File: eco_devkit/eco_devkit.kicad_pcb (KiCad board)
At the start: 2 copper layers, 24 parts, among them J10 Micro_SD_Card_Det1, J11 DISPLAY FFC, Q5 T2N7002AK,LM, Q6 SL2301S, U2 LTR-329ALS-01, U3 MC3419

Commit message: Add digital peripherals layout.
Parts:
- added BZ1: WT-1205, lib:buzzer, F.Cu at (211.0, 127.0)
- added C21: 0.1u, Capacitor_SMD:C_0402_1005Metric, F.Cu at (269.0, 152.0)
- added C22: 0.1u, Capacitor_SMD:C_0402_1005Metric, F.Cu at (269.0, 158.5)
- added C23: 0.1u, Capacitor_SMD:C_0402_1005Metric, F.Cu at (269.0, 165.0)
- added C24: 0.1u, Capacitor_SMD:C_0402_1005Metric, F.Cu at (269.0, 172.0)
- added D2: LED_Red, LED_SMD:LED_1206_3216Metric, F.Cu at (237.5, 124.0)
- added D3: LED_Green, LED_SMD:LED_1206_3216Metric, F.Cu at (237.5, 128.0)
- added D4: LED_Blue, LED_SMD:LED_1206_3216Metric, F.Cu at (237.5, 131.8)
- added D5: LED_Yellow, LED_SMD:LED_1206_3216Metric, F.Cu at (237.5, 135.5)
- added D6: WS2812B, LED_SMD:LED_WS2812B_PLCC4_5.0x5.0mm_P3.2mm, F.Cu at (238.0, 149.5)
- added D7: TSAL4400, LED_THT:LED_D3.0mm_Horizontal_O1.27mm_Z2.0mm, F.Cu at (208.2, 168.2)
- added J3: ADC_SEL1, Connector_PinSocket_2.54mm:PinSocket_1x02_P2.54mm_Vertical, F.Cu at (265.5, 129.0)
- added J4: BluetoothHeader, Connector_PinHeader_2.54mm:PinHeader_2x04_P2.54mm_Vertical, F.Cu at (236.5, 164.9)
- added Q1: MOSFET, Package_TO_SOT_SMD:SOT-23, F.Cu at (264.7, 123.9)
- added Q2: MMBT3904, Package_TO_SOT_SMD:SOT-523, F.Cu at (223.0, 125.1)
- added Q3: MOSFET, Package_TO_SOT_SMD:SOT-23, F.Cu at (209.0, 159.5)
- added Q4: OP598A, LED_THT:LED_D3.0mm_Horizontal_O1.27mm_Z2.0mm_Clear, F.Cu at (214.2, 168.2)
- added R12: 150, Resistor_SMD:R_0402_1005Metric, F.Cu at (241.5, 124.0)
- added R13: 150, Resistor_SMD:R_0402_1005Metric, F.Cu at (241.5, 128.0)
- added R14: 33, Resistor_SMD:R_0402_1005Metric, F.Cu at (241.5, 131.8)
- added R15: 150, Resistor_SMD:R_0402_1005Metric, F.Cu at (241.5, 135.5)
- added R16: 10k, Resistor_SMD:R_0402_1005Metric, F.Cu at (267.5, 152.0)
- added R17: 10k, Resistor_SMD:R_0402_1005Metric, F.Cu at (267.5, 158.5)
- added R18: 10k, Resistor_SMD:R_0402_1005Metric, F.Cu at (267.5, 165.0)
- added R19: 10k, Resistor_SMD:R_0402_1005Metric, F.Cu at (267.5, 172.0)
- added R20: 330, Resistor_SMD:R_0402_1005Metric, F.Cu at (240.5, 144.8)
- added R21: 100, Resistor_SMD:R_0402_1005Metric, F.Cu at (261.8, 123.5)
- added R22: 1k, Resistor_SMD:R_0402_1005Metric, F.Cu at (222.5, 122.5)
- added R23: 330, Resistor_SMD:R_0402_1005Metric, F.Cu at (208.1, 156.0)
- added R24: 10k, Resistor_SMD:R_0402_1005Metric, F.Cu at (233.0, 167.5)
- added R25: 220, Resistor_SMD:R_0402_1005Metric, F.Cu at (211.4, 161.5)
- added R26: 10k, Resistor_SMD:R_0402_1005Metric, F.Cu at (242.5, 165.0)
- added R27: 10k, Resistor_SMD:R_0402_1005Metric, F.Cu at (216.8, 161.5)
- added R28: 10k, Resistor_SMD:R_0402_1005Metric, F.Cu at (242.5, 170.0)
- added R29: 10k, Resistor_SMD:R_0402_1005Metric, F.Cu at (233.0, 172.5)
- added SW3: PTS636, Button_Switch_SMD:SW_Tactile_SPST_NO_Straight_CK_PTS636Sx25SMTRLFS, F.Cu at (262.0, 151.5)
- added SW4: PTS636, Button_Switch_SMD:SW_Tactile_SPST_NO_Straight_CK_PTS636Sx25SMTRLFS, F.Cu at (262.0, 158.0)
- added SW5: PTS636, Button_Switch_SMD:SW_Tactile_SPST_NO_Straight_CK_PTS636Sx25SMTRLFS, F.Cu at (262.0, 164.5)
- added SW6: PTS636, Button_Switch_SMD:SW_Tactile_SPST_NO_Straight_CK_PTS636Sx25SMTRLFS, F.Cu at (262.0, 171.5)
- moved C45 14.9 mm to (38.2, 179.1)
- moved C46 14.9 mm to (40.2, 179.1)
- moved C47 14.9 mm to (42.2, 179.1)
- moved J10 14.9 mm to (54.8, 162.6)
- moved C41 14.9 mm to (44.8, 164.6)
- moved C42 14.9 mm to (32.6, 162.8)
- moved C43 14.9 mm to (33.2, 173.1)
- moved C44 14.9 mm to (33.2, 174.1)
- moved C48 14.9 mm to (33.2, 186.6)
- moved C49 14.9 mm to (33.2, 185.6)
- moved J11 14.9 mm to (28.7, 179.1)
- moved JP1 14.9 mm to (48.0, 173.3)
- moved Q5 14.9 mm to (45.7, 189.1)
- moved Q6 14.9 mm to (44.6, 183.0)
- moved R42 14.9 mm to (44.8, 161.6)
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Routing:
- net Net-(D7-K): track 0.00 -> 7.78 mm
- net Net-(D7-A): track 0.00 -> 6.44 mm
- net IR_RX: track 0.00 -> 6.16 mm
- net Net-(BZ1--): track 0.00 -> 5.52 mm
- net GPIO_MOSFET_CONECTOR_OUT: track 0.00 -> 4.45 mm
- net PIN_BTN4: track 0.00 -> 3.13 mm
- net PIN_BTN3: track 0.00 -> 3.13 mm
- net PIN_BTN2: track 0.00 -> 3.13 mm
- net PIN_BTN1: track 0.00 -> 3.13 mm
- net Net-(J4-Pin_2): track 0.00 -> 3.02 mm
- net Net-(J4-Pin_6): track 0.00 -> 2.99 mm
- net PIN_WIFI_RESET_BL: track 0.00 -> 2.97 mm
- net Net-(J4-Pin_3): track 0.00 -> 2.97 mm
- net Net-(D6-DIN): track 0.00 -> 2.58 mm
- net Net-(D5-A): track 0.00 -> 2.09 mm
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
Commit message: Add probe.
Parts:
- added C26: 15p, Capacitor_SMD:C_0603_1608Metric, F.Cu at (110.0, 84.7)
- added C27: 15p, Capacitor_SMD:C_0603_1608Metric, F.Cu at (117.0, 86.2)
- added C28: 100n, Capacitor_SMD:C_0402_1005Metric, F.Cu at (109.5, 61.0)
- added C29: 10u, Capacitor_SMD:C_0402_1005Metric, F.Cu at (120.0, 63.0)
- added C30: 100n, Capacitor_SMD:C_0402_1005Metric, F.Cu at (115.5, 67.5)
- added C31: 100n, Capacitor_SMD:C_0402_1005Metric, F.Cu at (119.5, 67.5)
- added C32: 1u, Capacitor_SMD:C_0402_1005Metric, F.Cu at (119.9, 83.5)
- added C33: 100n, Capacitor_SMD:C_0402_1005Metric, F.Cu at (112.0, 72.5)
- added C34: 1u, Capacitor_SMD:C_0402_1005Metric, F.Cu at (112.0, 78.0)
- added C35: 100n, Capacitor_SMD:C_0402_1005Metric, F.Cu at (120.5, 67.5)
- added C36: 100n, Capacitor_SMD:C_0402_1005Metric, F.Cu at (121.5, 67.5)
- added C37: 100n, Capacitor_SMD:C_0402_1005Metric, F.Cu at (122.0, 74.5)
- added C38: 100n, Capacitor_SMD:C_0402_1005Metric, F.Cu at (122.0, 78.0)
- added C39: 100n, Capacitor_SMD:C_0402_1005Metric, F.Cu at (116.5, 67.5)
- added C40: 100n, Capacitor_SMD:C_0402_1005Metric, F.Cu at (118.5, 83.5)
- added D8: SB120, Diode_SMD:D_SOD-123F, F.Cu at (121.4, 61.0)
- added J2: Conn_02x20_Counter_Clockwise, Connector_PinHeader_2.54mm:PinHeader_2x20_P2.54mm_Vertical, F.Cu at (174.2, 126.0)
- added J8: USB_C_Receptacle_USB2.0_16P, lib:UJ20-C-H-G-SMT-1-P16-TR, F.Cu at (118.1, 50.2)
- added J9: SWD Interface, Connector_PinSocket_2.54mm:PinSocket_1x06_P2.54mm_Vertical, F.Cu at (105.0, 72.8)
- added MEM1: AT25EU0011A-SSHN-T, Footprint-FlashMEM:SOIC127P790X216-8N, F.Cu at (108.0, 65.0)
- added R35: DNF, Resistor_SMD:R_0402_1005Metric, F.Cu at (106.0, 61.0)
- added R36: 5.1k, Resistor_SMD:R_0402_1005Metric, F.Cu at (118.5, 61.5)
- added R37: 5.1k, Resistor_SMD:R_0402_1005Metric, F.Cu at (115.0, 61.5)
- added R38: 1k, Resistor_SMD:R_0402_1005Metric, F.Cu at (117.0, 83.2)
- added R39: 10k, Resistor_SMD:R_0402_1005Metric, F.Cu at (120.9, 83.5)
- added R40: 27, Resistor_SMD:R_0402_1005Metric, F.Cu at (117.5, 67.5)
- added R41: 27, Resistor_SMD:R_0402_1005Metric, F.Cu at (118.5, 67.5)
- added U1: RP2040, Package_DFN_QFN:QFN-56-1EP_7x7mm_P0.4mm_EP3.2x3.2mm_ThermalVias, F.Cu at (116.9, 75.9)
- added Y2: ABM8-272-T3, lib:ABM8-272-T3, F.Cu at (113.0, 84.2)
- moved R19 149.7 mm to (166.5, 61.5), turned to 0 degrees
- moved C24 149.6 mm to (166.5, 63.0), turned to 180 degrees
- moved SW6 149.6 mm to (167.0, 56.0), turned to -90 degrees
- moved R45 141.8 mm to (138.5, 68.8), turned to 90 degrees
- moved U3 141.2 mm to (138.0, 71.0), turned to 180 degrees
- moved U2 141.1 mm to (137.7, 74.6), turned to 90 degrees
- moved R44 140.4 mm to (137.5, 68.8), turned to 90 degrees
- moved R18 139.8 mm to (173.5, 61.5), turned to 0 degrees
- moved C23 139.7 mm to (173.5, 63.0), turned to 180 degrees
- moved SW5 139.7 mm to (174.0, 56.0), turned to -90 degrees
- moved C42 138.4 mm to (136.0, 70.8), turned to 90 degrees
- moved R17 130.6 mm to (180.0, 61.5), turned to 0 degrees
- moved SW4 130.6 mm to (180.5, 56.0), turned to -90 degrees
- moved C22 130.5 mm to (180.0, 63.0), turned to 180 degrees
- moved R48 122.1 mm to (124.3, 95.5), turned to -90 degrees
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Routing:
- net +3V3: track 0.00 -> 32.5 mm
- net /Debug Probe/QSPI_SS: track 0.00 -> 23.6 mm
- net /Debug Probe/RESET: track 0.00 -> 21.0 mm, vias 0 -> 1
- net /Debug Probe/SD1: track 0.00 -> 19.3 mm
- net /Debug Probe/SD2: track 0.00 -> 17.9 mm
- net /Debug Probe/SWDIO: track 0.00 -> 15.4 mm, vias 0 -> 1
- net /Debug Probe/SWCLK: track 0.00 -> 15.0 mm, vias 0 -> 1
- net +1V1: track 0.00 -> 14.5 mm
- net Net-(D8-A): track 0.00 -> 12.5 mm
- net /Debug Probe/SD3: track 0.00 -> 11.4 mm
- net /Debug Probe/QSPI_SCLK: track 0.00 -> 9.81 mm
- net /Debug Probe/XIN: track 0.00 -> 9.17 mm
- net /Debug Probe/SD0: track 0.00 -> 8.36 mm
- net Net-(C27-Pad2): track 0.00 -> 6.96 mm
- net Net-(U1-USB_DP): track 0.00 -> 4.65 mm
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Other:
- board outline added: 100 x 82 mm

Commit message: Placement v1.
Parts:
- added C1: 15p, Capacitor_SMD:C_0402_1005Metric, F.Cu at (124.2, 92.8)
- added C10: 4.7u, Capacitor_SMD:C_0402_1005Metric, F.Cu at (135.2, 70.4)
- added C11: 100n, Capacitor_SMD:C_0402_1005Metric, F.Cu at (116.4, 76.8)
- added C12: 100n, Capacitor_SMD:C_0402_1005Metric, F.Cu at (125.0, 68.6)
- added C13: 100n, Capacitor_SMD:C_0402_1005Metric, F.Cu at (116.4, 72.4)
- added C14: 100n, Capacitor_SMD:C_0402_1005Metric, F.Cu at (116.3, 74.5)
- added C15: 100n, Capacitor_SMD:C_0402_1005Metric, F.Cu at (116.3, 79.1)
- added C16: 100n, Capacitor_SMD:C_0402_1005Metric, F.Cu at (120.9, 84.2)
- added C17: 100n, Capacitor_SMD:C_0402_1005Metric, F.Cu at (122.8, 84.2)
- added C18: 100n, Capacitor_SMD:C_0402_1005Metric, F.Cu at (134.2, 75.0)
- added C19: 100n, Capacitor_SMD:C_0402_1005Metric, F.Cu at (134.3, 73.9)
- added C2: 15p, Capacitor_SMD:C_0402_1005Metric, F.Cu at (118.8, 92.7)
- added C20: 100n, Capacitor_SMD:C_0402_1005Metric, F.Cu at (134.2, 80.4)
- added C25: 1u, Capacitor_SMD:C_0402_1005Metric, F.Cu at (159.0, 121.0)
- added C3: 10u, Capacitor_SMD:C_0402_1005Metric, F.Cu at (111.8, 57.9)
- added C4: 100n, Capacitor_SMD:C_0402_1005Metric, F.Cu at (124.9, 64.1)
- added C5: 10u, Capacitor_SMD:C_0402_1005Metric, F.Cu at (111.6, 53.5)
- added C6: 4.7u, Capacitor_SMD:C_0402_1005Metric, F.Cu at (134.3, 72.8)
- added C7: 4.7u, Capacitor_SMD:C_0402_1005Metric, F.Cu at (130.5, 68.7)
- added C8: 100n, Capacitor_SMD:C_0402_1005Metric, F.Cu at (134.2, 76.5)
- added C9: 4.7u, Capacitor_SMD:C_0402_1005Metric, F.Cu at (125.1, 84.2)
- added D1: SB120, Diode_SMD:D_SOD-123F, F.Cu at (115.3, 60.2)
- added FLASH_MEMORY_8MB1: W25Q80DVSSIG, Package_SON:WSON-8-1EP_6x5mm_P1.27mm_EP3.4x4.3mm, F.Cu at (120.5, 66.5)
- added J1: USB_C_Receptacle_USB2.0_16P, lib:UJ20-C-H-G-SMT-1-P16-TR, F.Cu at (126.6, 50.0)
- added J5: ADC_SEL1, Connector_PinHeader_2.54mm:PinHeader_1x02_P2.54mm_Vertical, F.Cu at (188.5, 115.0)
- added J6: ADC_SEL1, Connector_PinHeader_2.54mm:PinHeader_1x02_P2.54mm_Vertical, F.Cu at (185.0, 115.0)
- added J7: ADC_SEL1, Connector_PinHeader_2.54mm:PinHeader_1x02_P2.54mm_Vertical, F.Cu at (181.5, 115.0)
- added L1: 3.3u, Inductor_SMD:L_0402_1005Metric, F.Cu at (129.0, 69.1)
- added MK1: MIC, EcoDevkit:MIC_CMEJ-0415-42-P, F.Cu at (159.0, 125.0)
- added NCP1: NCP1117ST50T3G, lib:NCP1117ST50T3G, F.Cu at (116.7, 53.9)
- added R1: 0, Resistor_SMD:R_0402_1005Metric, F.Cu at (115.0, 65.7)
- added R10: 27, Resistor_SMD:R_0402_1005Metric, F.Cu at (126.2, 68.6)
- added R11: 27, Resistor_SMD:R_0402_1005Metric, F.Cu at (127.5, 68.6)
- added R2: 0, Resistor_SMD:R_0402_1005Metric, F.Cu at (115.0, 64.6)
- added R3: 5.1k, Resistor_SMD:R_0402_1005Metric, F.Cu at (128.3, 59.1)
- added R30: 1k, Resistor_SMD:R_0402_1005Metric, F.Cu at (185.0, 126.0)
- added R31: 1k, Resistor_SMD:R_0402_1005Metric, F.Cu at (174.5, 126.0)
- added R32: 33k, Resistor_SMD:R_0402_1005Metric, F.Cu at (168.0, 120.0)
- added R33: 500k, OptoDevice:R_LDR_5.1x4.3mm_P3.4mm_Vertical, F.Cu at (168.0, 123.0)
- added R34: 2.2k, Resistor_SMD:R_0402_1005Metric, F.Cu at (159.0, 119.5)
- added R4: 5.1k, Resistor_SMD:R_0402_1005Metric, F.Cu at (124.3, 59.1)
- added R5: 10k, Resistor_SMD:R_0402_1005Metric, F.Cu at (115.0, 63.6)
- added R6: 1k, Resistor_SMD:R_0402_1005Metric, F.Cu at (125.4, 92.8)
- added R7: 1k, Resistor_SMD:R_0402_1005Metric, F.Cu at (117.6, 92.7)
- added R8: 33, Resistor_SMD:R_0402_1005Metric, F.Cu at (134.3, 71.6)
- added R9: 1k, Resistor_SMD:R_0402_1005Metric, F.Cu at (115.0, 66.7)
- added RP2350B1: RP2350B1, lib:RP2350B_QFN-80_EP_10.573x10.573_Pitch0.4mm, F.Cu at (123.6, 76.7)
- added RV1: 100k, EcoDevkit:TRIM_TC33X-2-203E, F.Cu at (188.0, 124.5)
- added RV2: 100k, EcoDevkit:TRIM_TC33X-2-203E, F.Cu at (177.5, 124.5)
- added SW1: BOOT, Button_Switch_SMD:SW_Tactile_SPST_NO_Straight_CK_PTS636Sx25SMTRLFS, F.Cu at (112.6, 73.4)
- added SW2: RESET, Button_Switch_SMD:SW_Tactile_SPST_NO_Straight_CK_PTS636Sx25SMTRLFS, F.Cu at (112.8, 92.7)
- added Y1: Crystal_GND24, lib:ABM8-272-T3, F.Cu at (121.5, 93.4)
- J11: footprint EcoDevkit:AMPHENOL_SFV28R-2STE1HLF -> EcoDevkit:FPC_30
- moved J2 96.2 mm to (103.1, 61.2), turned to 0 degrees
- moved J10 43.1 mm to (117.0, 120.8), turned to 0 degrees
- moved D2 42.7 mm to (164.5, 95.8), turned to 90 degrees
- moved D3 39.9 mm to (168.5, 95.8), turned to 90 degrees
- moved SW3 39.8 mm to (192.0, 95.5), turned to 180 degrees
- moved R12 38.1 mm to (164.5, 91.8), turned to 90 degrees
- moved R44 38.1 mm to (119.0, 102.0), turned to 180 degrees
- moved D4 37.9 mm to (172.3, 95.8), turned to 90 degrees
- moved R45 37.7 mm to (119.0, 101.0), turned to 180 degrees
- moved J3 37.2 mm to (162.9, 54.2), turned to 90 degrees
- moved J9 37.1 mm to (142.1, 72.0)
- moved R42 36.5 mm to (118.0, 110.8), turned to -90 degrees
- moved D5 36.5 mm to (176.0, 95.8), turned to 90 degrees
- moved C42 36.0 mm to (121.0, 103.5), turned to 180 degrees
- moved SW4 34.9 mm to (192.0, 89.0), turned to 180 degrees
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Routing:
- net +3V3: track 32.5 -> 76.5 mm
- net RUN: track 0.00 -> 17.3 mm
- net +1V1: track 14.5 -> 30.8 mm
- net PROBE_GPIO4/UART_TX: track 0.00 -> 16.1 mm
- net Net-(D1-A): track 0.00 -> 15.5 mm
- net /MCU/USB_D-: track 0.00 -> 13.8 mm
- net /MCU/XIN: track 0.00 -> 13.5 mm
- net /MCU/USB_D+: track 0.00 -> 13.5 mm
- net /MCU/QSPI_SS: track 0.00 -> 12.6 mm
- net /MCU/XOUT: track 0.00 -> 11.3 mm
- net /MCU/QSPI_SD1: track 0.00 -> 10.7 mm
- net Net-(RP2350B1-VREG_AVDD): track 0.00 -> 9.75 mm
- net /MCU/QSPI_SD2: track 0.00 -> 7.97 mm
- net Net-(R7-Pad2): track 0.00 -> 7.02 mm
- net +VBUS: track 0.00 -> 6.81 mm
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- added copper zone on F.Cu, net (none)
- added copper zone on F.Cu, net +3V3
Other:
- board size 100 x 82 mm -> 98.5 x 78 mm

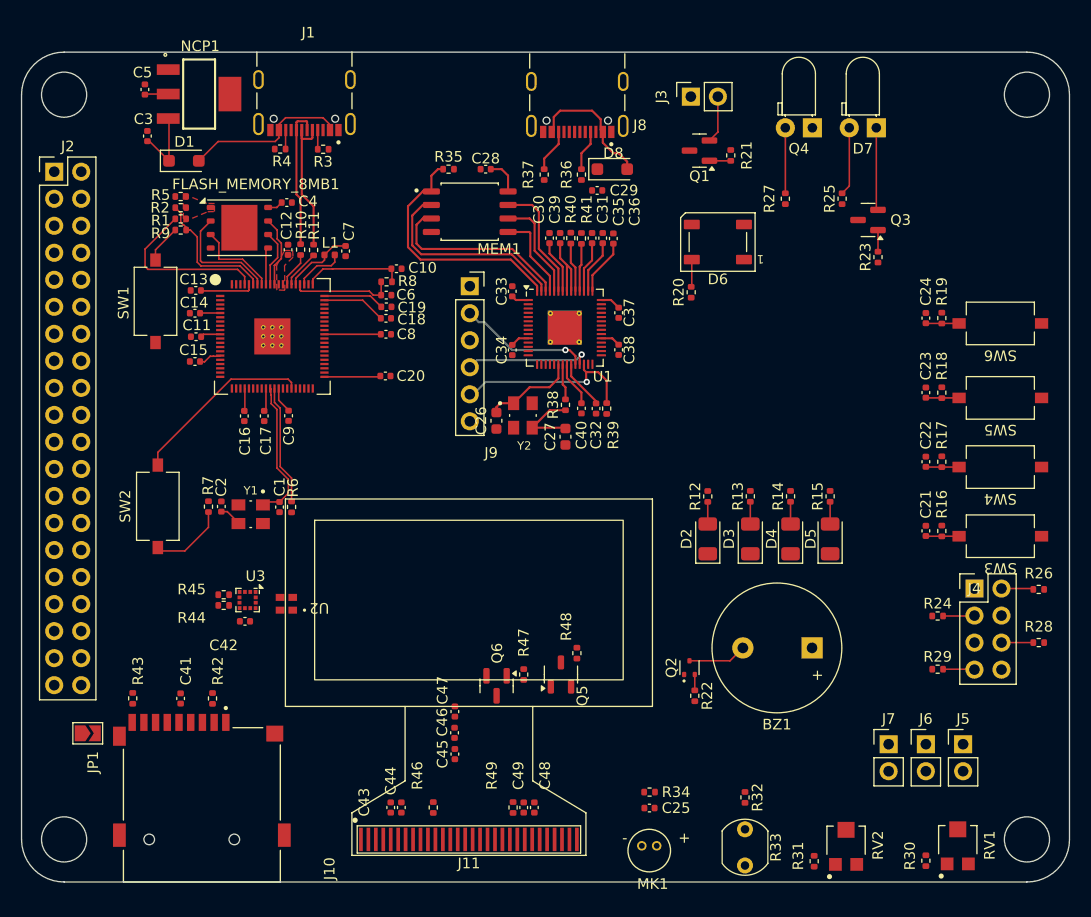
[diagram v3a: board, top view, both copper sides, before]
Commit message: fix:adjustments to component placement and routing
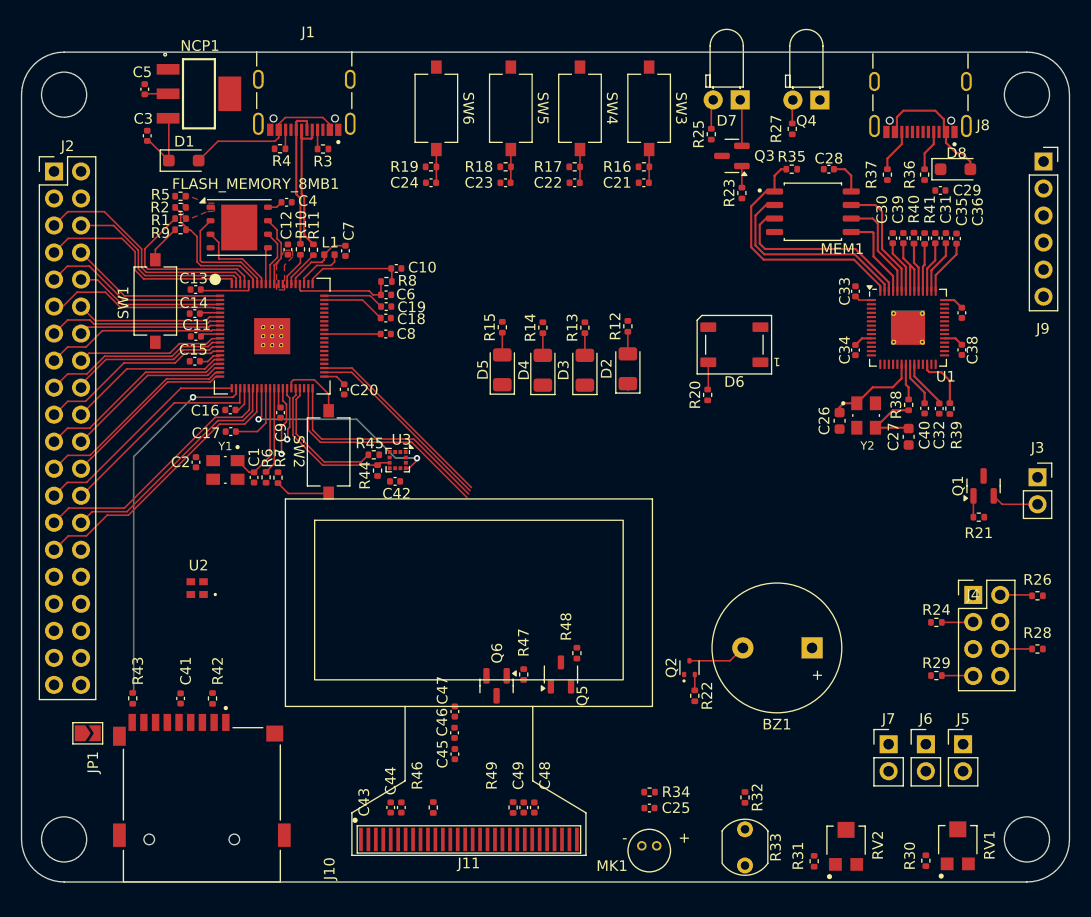
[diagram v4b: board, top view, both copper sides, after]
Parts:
- moved SW6 56.7 mm to (139.0, 55.3), turned to -90 degrees
- moved J9 55.2 mm to (196.1, 60.3)
- moved SW5 53.5 mm to (146.0, 55.3), turned to -90 degrees
- moved SW3 52.0 mm to (159.0, 55.3), turned to -90 degrees
- moved SW4 51.9 mm to (152.5, 55.3), turned to -90 degrees
- moved R19 50.1 mm to (138.5, 60.8), turned to 0 degrees
- moved J3 48.4 mm to (195.5, 90.0), turned to 0 degrees
- moved C24 48.2 mm to (138.5, 62.3), turned to 180 degrees
- moved R18 46.2 mm to (145.5, 60.8), turned to 0 degrees
- moved R17 44.3 mm to (152.0, 60.8), turned to 0 degrees
- moved R16 44.2 mm to (158.5, 60.8), turned to 0 degrees
- moved C23 44.2 mm to (145.5, 62.3), turned to 180 degrees
- moved C22 42.2 mm to (152.0, 62.3), turned to 180 degrees
- moved C21 42.1 mm to (158.5, 62.3), turned to 180 degrees
- moved Q1 41.3 mm to (190.4, 90.8), turned to 90 degrees
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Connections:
- J2 pad 21: PROBE_GPIO2/SWCLK -> /MCU/GPIO17
- J2 pad 22: SWD -> ACCEL_SCK
- J2 pad 23: RUN -> ACCEL_MOSI
- J2 pad 24: GPIO43_ADC3 -> ACCEL_MISO
- J2 pad 25: GPIO46_ADC6 -> GPIO21
- J2 pad 26: GPIO45_ADC5 -> /MCU/GPIO23
- J2 pad 27: GPIO44_ADC4 -> /MCU/GPIO24
- J2 pad 28: GPIO43_ADC3 -> /MCU/GPIO25
- J2 pad 29: GPIO42_ADC2 -> PIN_BUZZER
- J2 pad 30: GPIO41_ADC1 -> GPIO40_ADC0
- J2 pad 31: GPIO40_ADC0 -> GPIO41_ADC1
- J2 pad 32: PIN_BUZZER -> GPIO42_ADC2
- J2 pad 33: /MCU/GPIO25 -> GPIO43_ADC3
- J2 pad 34: /MCU/GPIO24 -> GPIO44_ADC4
- J2 pad 35: /MCU/GPIO23 -> GPIO45_ADC5
- J2 pad 36: GPIO21 -> GPIO46_ADC6
- J2 pad 37: ACCEL_MISO -> PROBE_GPIO2/SWCLK
- J2 pad 38: ACCEL_MOSI -> SWD
- J2 pad 39: ACCEL_SCK -> RUN
- J2 pad 40: /MCU/GPIO17 -> GPIO43_ADC3
- RP2350B1 pad 30: /MCU/XOUT -> /MCU/XIN
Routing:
- net GPIO22: track 0.00 -> 34.8 mm, vias 0 -> 1
- net PIN_BUZZER: track 0.00 -> 26.7 mm
- net /MCU/GPIO24: track 0.00 -> 24.8 mm
- net /MCU/GPIO25: track 0.00 -> 22.7 mm
- net POBRE_GPIO5/UART_RX: track 0.00 -> 22.3 mm
- net PIN_LED_RED: track 0.00 -> 22.2 mm
- net PIN_LED_GREEN: track 0.00 -> 21.6 mm
- net ACCEL_CS: track 0.00 -> 21.0 mm, vias 0 -> 2
- net GPIO21: track 0.00 -> 20.9 mm
- net /MCU/GPIO3: track 0.10 -> 20.4 mm
- net /MCU/GPIO23: track 0.00 -> 19.9 mm
- net ACCEL_MOSI: track 0.00 -> 19.4 mm
- net PIN_LED_YELLOW: track 0.00 -> 19.0 mm
- net PIN_LED_BLUE: track 0.00 -> 18.7 mm
- net /MCU/GPIO17: track 0.00 -> 18.6 mm
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
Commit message: Update layout
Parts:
- moved J3 47.7 mm to (166.0, 52.5), turned to 90 degrees
- moved Q4 47.0 mm to (194.7, 97.3), turned to 90 degrees
- moved D7 44.5 mm to (194.7, 89.8), turned to 90 degrees
- moved R27 42.2 mm to (191.9, 94.7), turned to 180 degrees
- moved R21 41.0 mm to (169.8, 58.0), turned to 90 degrees
- moved Q1 40.7 mm to (166.8, 57.6), turned to 180 degrees
- moved R25 39.6 mm to (191.4, 87.0), turned to 0 degrees
- moved Q3 37.0 mm to (189.4, 89.0), turned to 90 degrees
- moved R23 32.3 mm to (185.9, 89.9), turned to 0 degrees
- moved C43 2.20 mm to (132.5, 121.0), turned to 180 degrees
- moved C48 1.52 mm to (148.2, 119.5), turned to -90 degrees
- moved C49 1.52 mm to (147.2, 119.5), turned to -90 degrees
- moved R49 1.52 mm to (146.2, 119.5), turned to -90 degrees
- moved R45 1.11 mm to (132.0, 87.8), turned to -90 degrees
- moved D6 1.00 mm to (167.0, 78.5)
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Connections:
- J2 pad 18: /MCU/GPIO14 -> DISPLAY_CS
- J2 pad 20: /MCU/GPIO16 -> IR_RX
- J2 pad 21: /MCU/GPIO17 -> IR_TX
- RP2350B1 pad 13: /MCU/GPIO14 -> DISPLAY_CS
- RP2350B1 pad 16: /MCU/GPIO16 -> IR_RX
- RP2350B1 pad 17: /MCU/GPIO17 -> IR_TX
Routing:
- net IR_RX: track 2.23 -> 138.4 mm, vias 0 -> 2
- net IR_TX: track 0.00 -> 132.9 mm, vias 0 -> 2
- net DISPLAY_EN: track 17.4 -> 113.0 mm, vias 0 -> 2
- net DISPLAY_CS: track 0.00 -> 86.6 mm, vias 0 -> 2
- net POBRE_GPIO5/UART_RX: track 22.3 -> 107.6 mm, vias 0 -> 2
- net PROBE_GPIO4/UART_TX: track 16.1 -> 97.3 mm, vias 0 -> 2
- net DISPLAY_RST: track 13.9 -> 91.9 mm, vias 0 -> 2
- net PROBE_GPIO2/SWCLK: track 6.55 -> 73.4 mm, vias 1 -> 2
- net POBRE_GPIO3/SWDIO: track 5.02 -> 70.3 mm, vias 1 -> 0
- net PIN_BUZZER: track 26.7 -> 89.8 mm
- net GPIO_MOSFET_GATE_IN: track 0.00 -> 58.1 mm, vias 0 -> 2
- net ACCEL_MOSI: track 19.4 -> 57.9 mm, vias 0 -> 2
- net PIN_BTN1: track 3.13 -> 41.6 mm
- net ACCEL_SCK: track 15.9 -> 49.4 mm, vias 0 -> 2
- net ACCEL_MISO: track 16.7 -> 50.2 mm, vias 0 -> 2
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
